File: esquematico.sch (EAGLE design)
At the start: 7 parts, among them IC1 MIC5219FMM, K1 CQ1-12V, T1 BC337

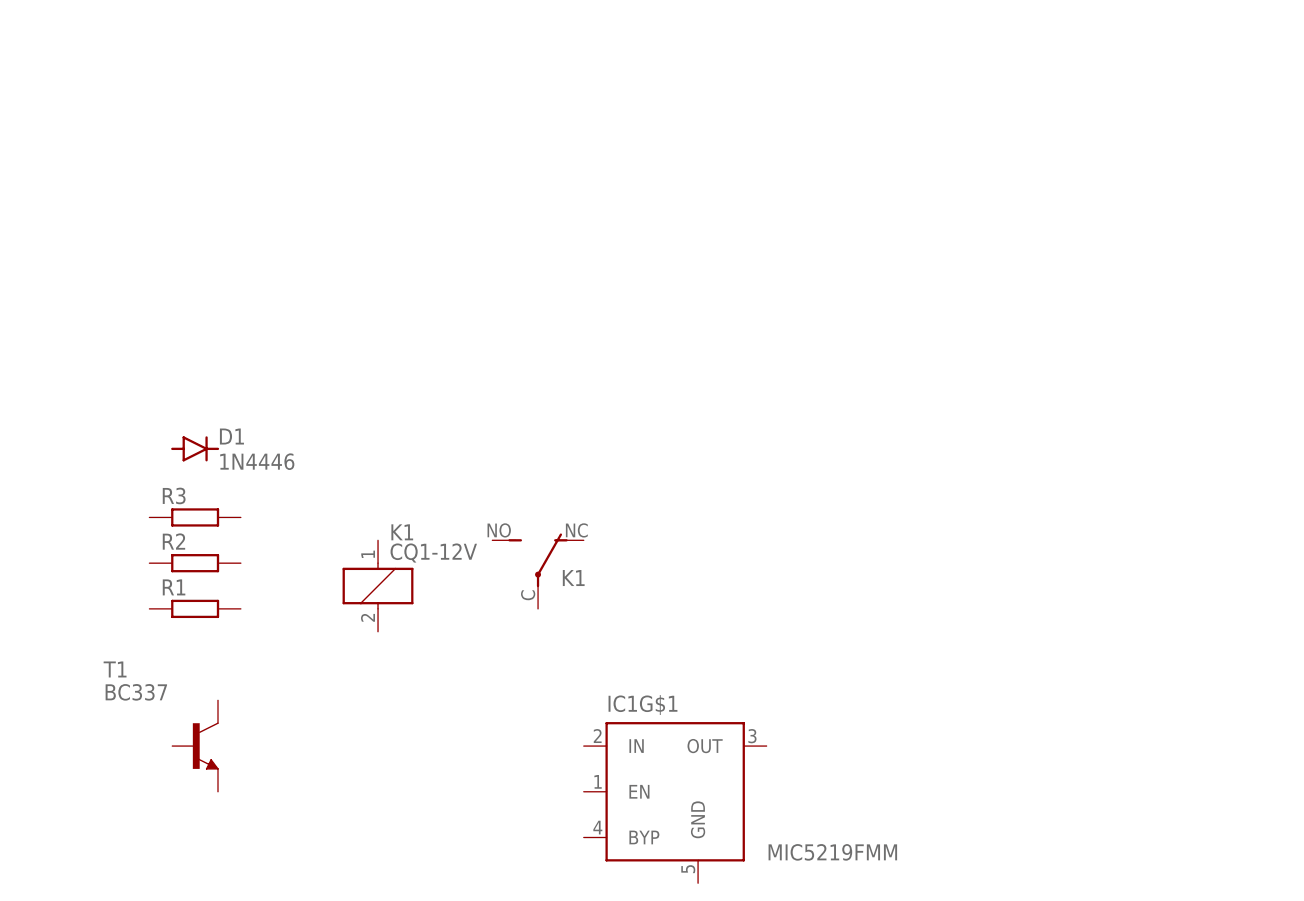
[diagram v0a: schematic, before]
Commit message: Se termina RTC, REG.voltaje y Rele
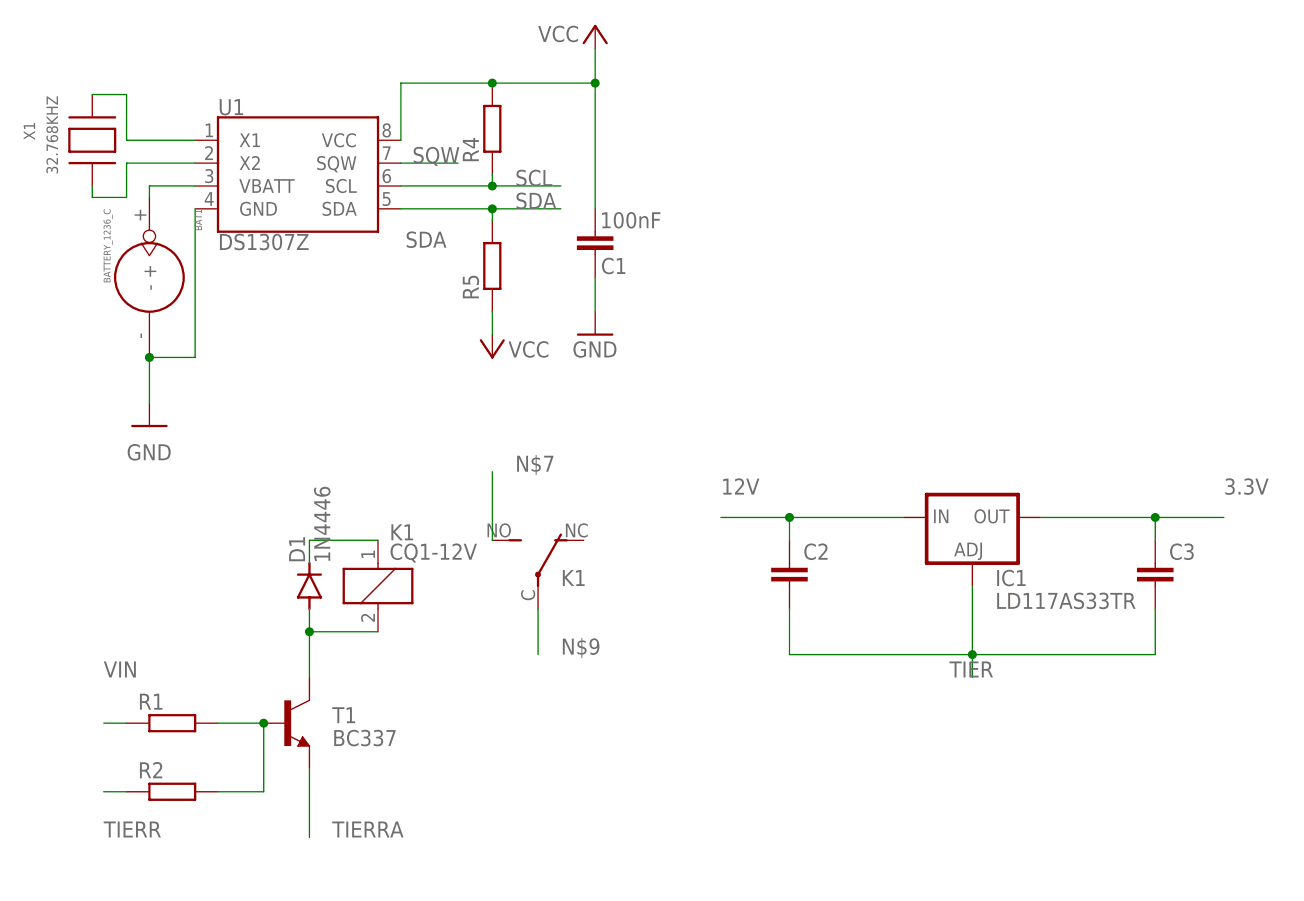
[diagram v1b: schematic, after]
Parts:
- removed R3: (no value), rcl:R-EU_0207/10
- added BAT1: BATTERY_1236_C, Itead_BP_110825.lbr:BATTERY_1236_C
- added C1: 100nF, rcl:C-EUC0603
- added C2, C3: (no value), rcl:C-EU050-025X075
- added R4, R5: (no value), rcl:R-EU_0207/10
- added U1: DS1307Z, SparkFun-Clocks:DS1307Z
- added X1: 32.768KHZ, adafruit:XTAL-3.2X1.5
- IC1: value MIC5219FMM -> LD117AS33TR; device v-reg-micrel:MIC5219FMM -> v-reg:LD117AS33TR
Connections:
- new net 12V: C2.1, IC1.IN
- new net 3.3V: C3.1, IC1.OUT
- new net GND: BAT1.-, C1.1, U1.GND
- new net N$1: U1.X1, X1.P$2
- new net N$2: U1.X2, X1.P$1
- new net N$3: D1.A, K11.2, T1.C
- new net N$4: BAT1.+, U1.VBATT
- new net N$5: D1.C, K11.1
- new net N$6: R1.2, R2.2, T1.B
- new net N$7: K12.S
- new net N$9: K12.P
- new net SCL: R4.1, U1.SCL
- new net SDA: R5.2, U1.SDA
- new net SQW: U1.SQW
- new net TIER: C2.2, C3.2, IC1.ADJ
- new net TIERR: R2.1
- new net TIERRA: T1.E
- new net VCC: C1.2, R4.2, R5.1, U1.VCC
- new net VIN: R1.1
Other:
- moved on the sheet: D1, R1, R2, T1
